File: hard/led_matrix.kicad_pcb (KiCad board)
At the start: 2 copper layers, 1 part

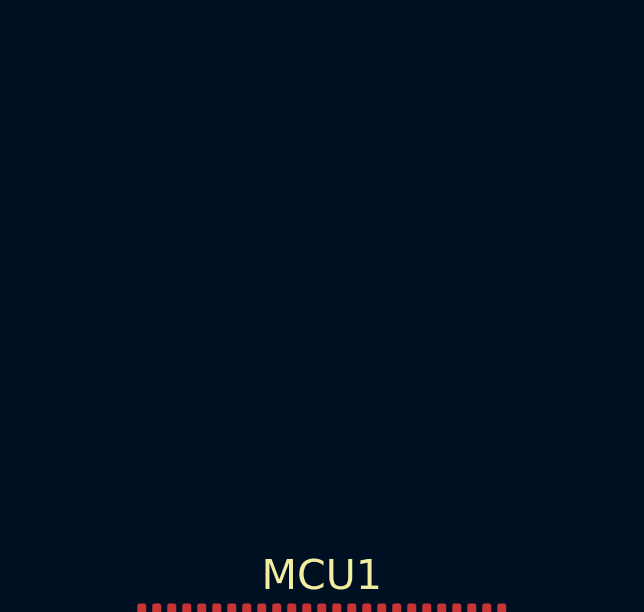
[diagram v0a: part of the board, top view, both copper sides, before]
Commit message: added 3d model for dc dc inductor
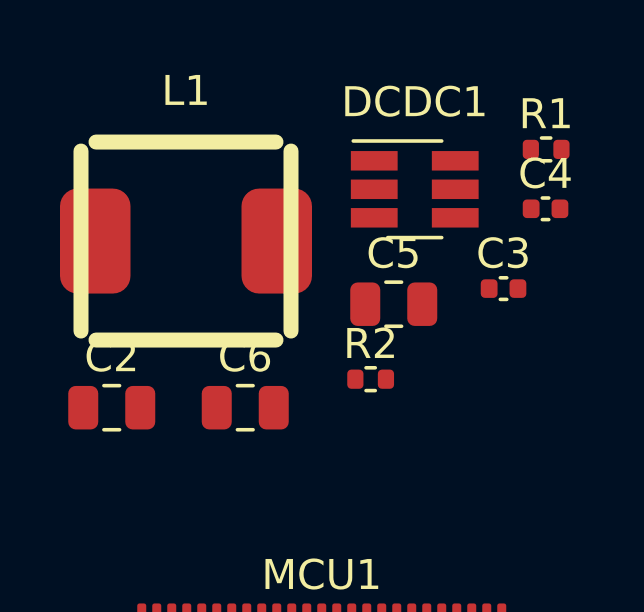
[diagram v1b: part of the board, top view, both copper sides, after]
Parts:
- added C2: 22u/16V, Capacitor_SMD:C_0805_2012Metric, F.Cu at (115.0, 70.0)
- added C3: 100n/16V, Capacitor_SMD:C_0402_1005Metric, F.Cu at (128.1, 66.0)
- added C4: 68p, Capacitor_SMD:C_0402_1005Metric, F.Cu at (129.5, 63.4)
- added C5: 22u/16V, Capacitor_SMD:C_0805_2012Metric, F.Cu at (124.4, 66.5)
- added C6: 22u/16V, Capacitor_SMD:C_0805_2012Metric, F.Cu at (119.5, 70.0)
- added DCDC1: TPS54302DDCR, Package_TO_SOT_SMD:SOT-23-6_Handsoldering, F.Cu at (125.1, 62.7)
- added L1: 8u2, led_matrix:L_Sunking_MWSA0603S, F.Cu at (117.5, 64.4)
- added R1: 100K/1%, Resistor_SMD:R_0402_1005Metric, F.Cu at (129.5, 61.4)
- added R2: 22K/1%, Resistor_SMD:R_0402_1005Metric, F.Cu at (123.6, 69.0)

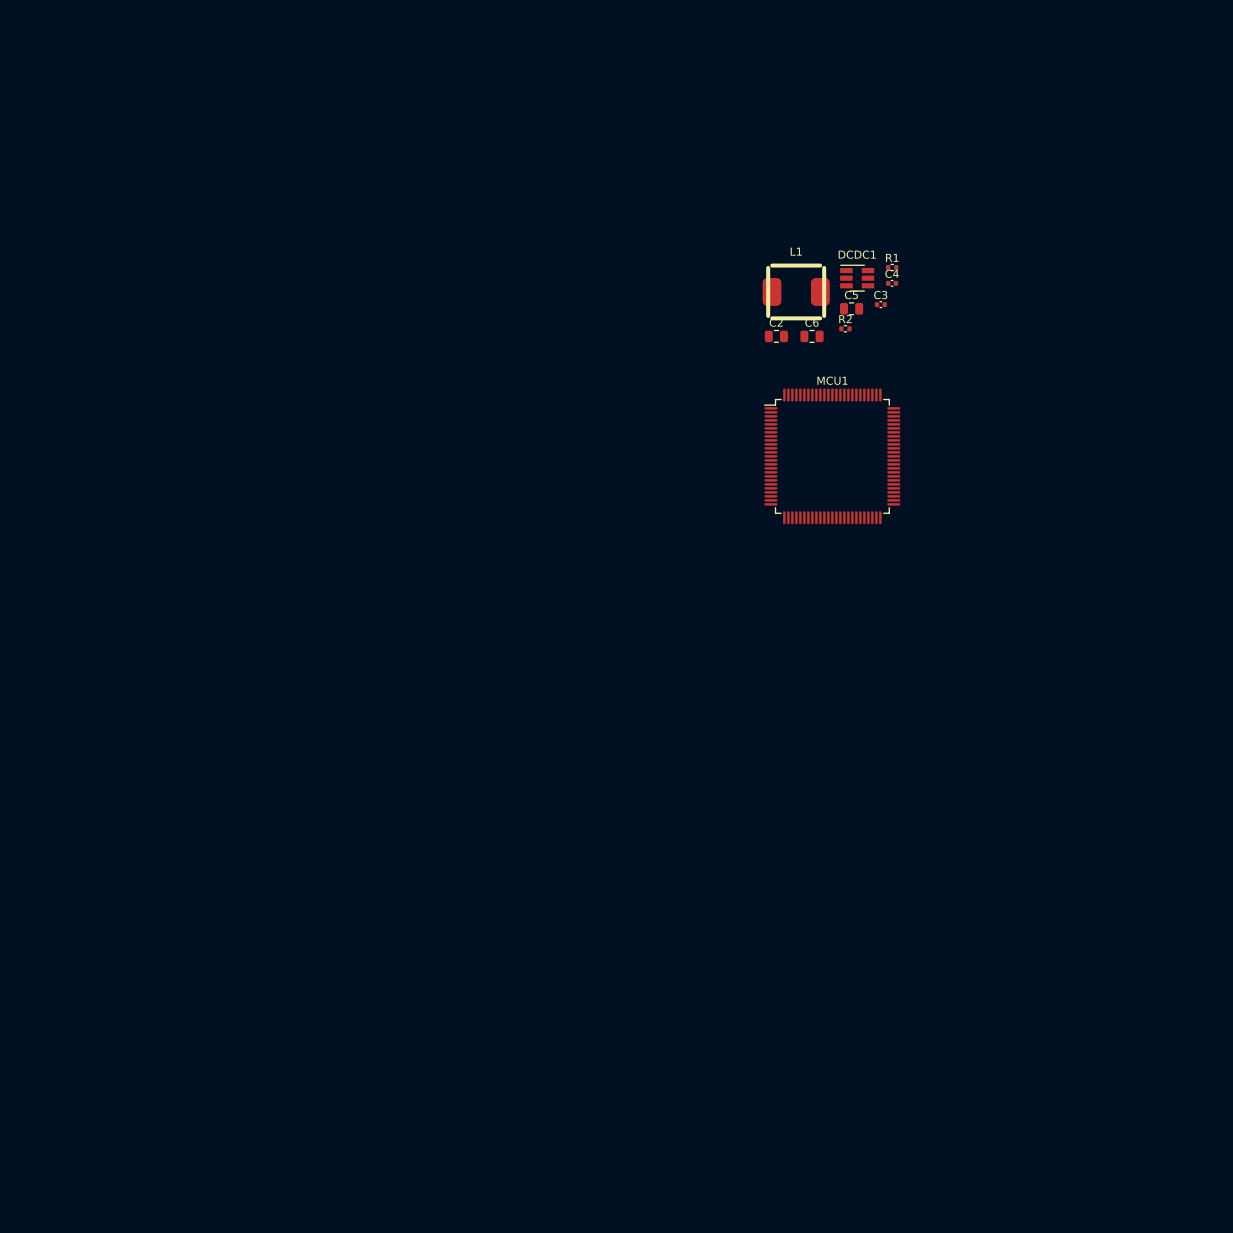
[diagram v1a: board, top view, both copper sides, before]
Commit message: signal nmos added
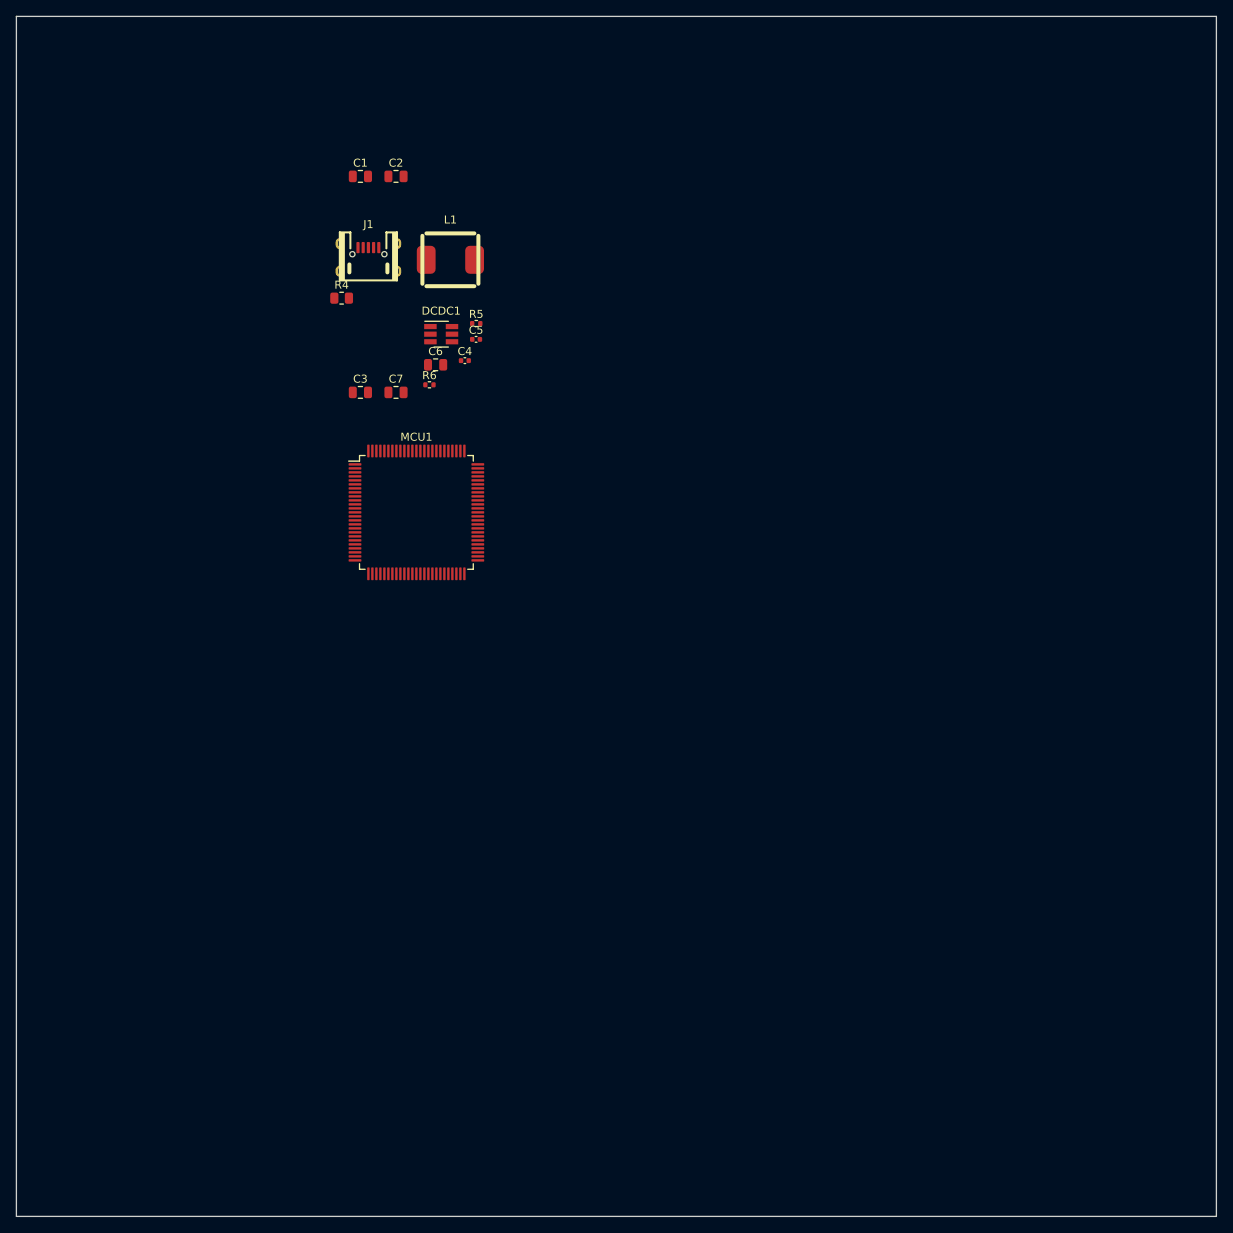
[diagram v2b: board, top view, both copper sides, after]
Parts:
- removed R1: 100K/1%, Resistor_SMD:R_0402_1005Metric
- removed R2: 22K/1%, Resistor_SMD:R_0402_1005Metric
- added C1: 22u/16V, Capacitor_SMD:C_0805_2012Metric, F.Cu at (63.0, 50.0)
- added C7: 22u/16V, Capacitor_SMD:C_0805_2012Metric, F.Cu at (67.5, 77.0)
- added J1: MicroXNJ, led_matrix:Connectors_SHOU HAN_MICRO 4P DIP, F.Cu at (64.0, 63.0)
- added R4: 0R1, Resistor_SMD:R_0805_2012Metric, F.Cu at (60.7, 65.2)
- added R5: 100K/1%, Resistor_SMD:R_0402_1005Metric, F.Cu at (77.5, 68.4)
- added R6: 22K/1%, Resistor_SMD:R_0402_1005Metric, F.Cu at (71.6, 76.0)
- C3: value 100n/16V -> 22u/16V; footprint Capacitor_SMD:C_0402_1005Metric -> Capacitor_SMD:C_0805_2012Metric
- C4: value 68p -> 100n/16V
- C5: value 22u/16V -> 68p; footprint Capacitor_SMD:C_0805_2012Metric -> Capacitor_SMD:C_0402_1005Metric
- moved C3 66.0 mm to (63.0, 77.0)
- moved C4 54.3 mm to (76.1, 73.0)
- moved DCDC1 52.5 mm to (73.1, 69.7)
- moved MCU1 52.5 mm to (70.0, 92.0)
- moved C2 51.6 mm to (67.5, 50.0)
- moved C6 47.2 mm to (72.4, 73.5)
- moved C5 47.1 mm to (77.5, 70.4)
- moved L1 43.4 mm to (74.2, 60.4)
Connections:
- C3 pad 1: Net-(C3-Pad1) -> GND
- C3 pad 2: Net-(C3-Pad2) -> +5V
- C4 pad 2: +3V3 -> Net-(C4-Pad2)
- C5 pad 1: GND -> Net-(C5-Pad1)
- DCDC1 pad 2: Net-(C3-Pad1) -> Net-(C4-Pad1)
- DCDC1 pad 4: Net-(C4-Pad1) -> Net-(C5-Pad1)
- DCDC1 pad 6: Net-(C3-Pad2) -> Net-(C4-Pad2)
- L1 pad 1: Net-(C3-Pad1) -> Net-(C4-Pad1)
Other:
- board outline added: 150 x 150 mm

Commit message: RIIIIIIIIIIIIIBSSSSSS!!!!
Rib break
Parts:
- added D1: LTST-S270TBKT, led_matrix:LED_LiteOn_LTST-S270TBKT, F.Cu at (74.3, 177.2)
- added D10: LTST-S270TBKT, led_matrix:LED_LiteOn_LTST-S270TBKT, F.Cu at (52.3, 137.3)
- added D100: LTST-S270TBKT, led_matrix:LED_LiteOn_LTST-S270TBKT, F.Cu at (78.7, 139.4)
- added D1000: LTST-S270TBKT, led_matrix:LED_LiteOn_LTST-S270TBKT, F.Cu at (179.9, 154.1)
- added D1001: LTST-S270TBKT, led_matrix:LED_LiteOn_LTST-S270TBKT, F.Cu at (175.5, 158.3)
- added D1002: LTST-S270TBKT, led_matrix:LED_LiteOn_LTST-S270TBKT, F.Cu at (171.1, 162.5)
- added D1003: LTST-S270TBKT, led_matrix:LED_LiteOn_LTST-S270TBKT, F.Cu at (166.7, 166.7)
- added D1004: LTST-S270TBKT, led_matrix:LED_LiteOn_LTST-S270TBKT, F.Cu at (162.3, 170.9)
- added D1005: LTST-S270TBKT, led_matrix:LED_LiteOn_LTST-S270TBKT, F.Cu at (157.9, 175.1)
- added D1006: LTST-S270TBKT, led_matrix:LED_LiteOn_LTST-S270TBKT, F.Cu at (153.5, 179.3)
- added D1007: LTST-S270TBKT, led_matrix:LED_LiteOn_LTST-S270TBKT, F.Cu at (122.7, 210.8)
- added D1008: LTST-S270TBKT, led_matrix:LED_LiteOn_LTST-S270TBKT, F.Cu at (127.1, 206.6)
- added D1009: LTST-S270TBKT, led_matrix:LED_LiteOn_LTST-S270TBKT, F.Cu at (113.9, 210.8)
- added D101: LTST-S270TBKT, led_matrix:LED_LiteOn_LTST-S270TBKT, F.Cu at (83.1, 137.3)
- added D1010: LTST-S270TBKT, led_matrix:LED_LiteOn_LTST-S270TBKT, F.Cu at (135.9, 198.2)
- added D1011: LTST-S270TBKT, led_matrix:LED_LiteOn_LTST-S270TBKT, F.Cu at (140.3, 194.0)
- added D1012: LTST-S270TBKT, led_matrix:LED_LiteOn_LTST-S270TBKT, F.Cu at (144.7, 189.8)
- added D1013: LTST-S270TBKT, led_matrix:LED_LiteOn_LTST-S270TBKT, F.Cu at (149.1, 185.6)
- added D1014: LTST-S270TBKT, led_matrix:LED_LiteOn_LTST-S270TBKT, F.Cu at (149.1, 187.7)
- added D1015: LTST-S270TBKT, led_matrix:LED_LiteOn_LTST-S270TBKT, F.Cu at (144.7, 191.9)
- added D1016: LTST-S270TBKT, led_matrix:LED_LiteOn_LTST-S270TBKT, F.Cu at (140.3, 196.1)
- added D1017: LTST-S270TBKT, led_matrix:LED_LiteOn_LTST-S270TBKT, F.Cu at (135.9, 200.3)
- added D1018: LTST-S270TBKT, led_matrix:LED_LiteOn_LTST-S270TBKT, F.Cu at (131.5, 204.5)
- added D1019: LTST-S270TBKT, led_matrix:LED_LiteOn_LTST-S270TBKT, F.Cu at (127.1, 208.7)
- added D102: LTST-S270TBKT, led_matrix:LED_LiteOn_LTST-S270TBKT, F.Cu at (78.7, 141.5)
- added D1020: LTST-S270TBKT, led_matrix:LED_LiteOn_LTST-S270TBKT, F.Cu at (122.7, 212.9)
- added D1021: LTST-S270TBKT, led_matrix:LED_LiteOn_LTST-S270TBKT, F.Cu at (153.5, 181.4)
- added D1022: LTST-S270TBKT, led_matrix:LED_LiteOn_LTST-S270TBKT, F.Cu at (157.9, 177.2)
- added D1023: LTST-S270TBKT, led_matrix:LED_LiteOn_LTST-S270TBKT, F.Cu at (162.3, 173.0)
- added D1024: LTST-S270TBKT, led_matrix:LED_LiteOn_LTST-S270TBKT, F.Cu at (166.7, 168.8)
- added D103: LTST-S270TBKT, led_matrix:LED_LiteOn_LTST-S270TBKT, F.Cu at (74.3, 145.7)
- added D104: LTST-S270TBKT, led_matrix:LED_LiteOn_LTST-S270TBKT, F.Cu at (69.9, 149.9)
- added D105: LTST-S270TBKT, led_matrix:LED_LiteOn_LTST-S270TBKT, F.Cu at (65.5, 154.1)
- added D106: LTST-S270TBKT, led_matrix:LED_LiteOn_LTST-S270TBKT, F.Cu at (61.1, 158.3)
- added D107: LTST-S270TBKT, led_matrix:LED_LiteOn_LTST-S270TBKT, F.Cu at (56.7, 162.5)
- added D108: LTST-S270TBKT, led_matrix:LED_LiteOn_LTST-S270TBKT, F.Cu at (52.3, 166.7)
- added D109: LTST-S270TBKT, led_matrix:LED_LiteOn_LTST-S270TBKT, F.Cu at (47.9, 170.9)
- added D11: LTST-S270TBKT, led_matrix:LED_LiteOn_LTST-S270TBKT, F.Cu at (47.9, 141.5)
- added D110: LTST-S270TBKT, led_matrix:LED_LiteOn_LTST-S270TBKT, F.Cu at (25.7, 120.5)
- added D111: LTST-S270TBKT, led_matrix:LED_LiteOn_LTST-S270TBKT, F.Cu at (87.5, 135.2)
- added D112: LTST-S270TBKT, led_matrix:LED_LiteOn_LTST-S270TBKT, F.Cu at (25.7, 125.0)
- added D113: LTST-S270TBKT, led_matrix:LED_LiteOn_LTST-S270TBKT, F.Cu at (65.5, 139.4)
- added D114: LTST-S270TBKT, led_matrix:LED_LiteOn_LTST-S270TBKT, F.Cu at (52.3, 168.8)
- added D115: LTST-S270TBKT, led_matrix:LED_LiteOn_LTST-S270TBKT, F.Cu at (56.7, 164.6)
- added D116: LTST-S270TBKT, led_matrix:LED_LiteOn_LTST-S270TBKT, F.Cu at (61.1, 160.4)
- added D117: LTST-S270TBKT, led_matrix:LED_LiteOn_LTST-S270TBKT, F.Cu at (65.5, 156.2)
- added D118: LTST-S270TBKT, led_matrix:LED_LiteOn_LTST-S270TBKT, F.Cu at (69.9, 152.0)
- added D119: LTST-S270TBKT, led_matrix:LED_LiteOn_LTST-S270TBKT, F.Cu at (74.3, 147.8)
- added D12: LTST-S270TBKT, led_matrix:LED_LiteOn_LTST-S270TBKT, F.Cu at (25.7, 57.0)
- added D120: LTST-S270TBKT, led_matrix:LED_LiteOn_LTST-S270TBKT, F.Cu at (78.7, 143.6)
- added D121: LTST-S270TBKT, led_matrix:LED_LiteOn_LTST-S270TBKT, F.Cu at (83.1, 139.4)
- added D122: LTST-S270TBKT, led_matrix:LED_LiteOn_LTST-S270TBKT, F.Cu at (87.5, 137.3)
- added D123: LTST-S270TBKT, led_matrix:LED_LiteOn_LTST-S270TBKT, F.Cu at (83.1, 141.5)
- added D124: LTST-S270TBKT, led_matrix:LED_LiteOn_LTST-S270TBKT, F.Cu at (78.7, 145.7)
- added D125: LTST-S270TBKT, led_matrix:LED_LiteOn_LTST-S270TBKT, F.Cu at (74.3, 149.9)
- added D126: LTST-S270TBKT, led_matrix:LED_LiteOn_LTST-S270TBKT, F.Cu at (69.9, 154.1)
- added D127: LTST-S270TBKT, led_matrix:LED_LiteOn_LTST-S270TBKT, F.Cu at (65.5, 158.3)
- added D128: LTST-S270TBKT, led_matrix:LED_LiteOn_LTST-S270TBKT, F.Cu at (61.1, 162.5)
- added D129: LTST-S270TBKT, led_matrix:LED_LiteOn_LTST-S270TBKT, F.Cu at (74.3, 160.4)
- added D13: LTST-S270TBKT, led_matrix:LED_LiteOn_LTST-S270TBKT, F.Cu at (56.7, 135.2)
- added D130: LTST-S270TBKT, led_matrix:LED_LiteOn_LTST-S270TBKT, F.Cu at (52.3, 170.9)
- added D131: LTST-S270TBKT, led_matrix:LED_LiteOn_LTST-S270TBKT, F.Cu at (47.9, 175.1)
- added D132: LTST-S270TBKT, led_matrix:LED_LiteOn_LTST-S270TBKT, F.Cu at (25.7, 129.5)
- added D133: LTST-S270TBKT, led_matrix:LED_LiteOn_LTST-S270TBKT, F.Cu at (91.9, 135.2)
- added D134: LTST-S270TBKT, led_matrix:LED_LiteOn_LTST-S270TBKT, F.Cu at (25.7, 134.1)
- added D135: LTST-S270TBKT, led_matrix:LED_LiteOn_LTST-S270TBKT, F.Cu at (47.9, 177.2)
- added D136: LTST-S270TBKT, led_matrix:LED_LiteOn_LTST-S270TBKT, F.Cu at (52.3, 173.0)
- added D137: LTST-S270TBKT, led_matrix:LED_LiteOn_LTST-S270TBKT, F.Cu at (56.7, 168.8)
- added D138: LTST-S270TBKT, led_matrix:LED_LiteOn_LTST-S270TBKT, F.Cu at (61.1, 164.6)
- added D139: LTST-S270TBKT, led_matrix:LED_LiteOn_LTST-S270TBKT, F.Cu at (65.5, 160.4)
- added D14: LTST-S270TBKT, led_matrix:LED_LiteOn_LTST-S270TBKT, F.Cu at (25.7, 61.5)
- added D140: LTST-S270TBKT, led_matrix:LED_LiteOn_LTST-S270TBKT, F.Cu at (69.9, 156.2)
- added D141: LTST-S270TBKT, led_matrix:LED_LiteOn_LTST-S270TBKT, F.Cu at (74.3, 152.0)
- added D142: LTST-S270TBKT, led_matrix:LED_LiteOn_LTST-S270TBKT, F.Cu at (78.7, 147.8)
- added D143: LTST-S270TBKT, led_matrix:LED_LiteOn_LTST-S270TBKT, F.Cu at (83.1, 143.6)
- added D144: LTST-S270TBKT, led_matrix:LED_LiteOn_LTST-S270TBKT, F.Cu at (87.5, 139.4)
- added D145: LTST-S270TBKT, led_matrix:LED_LiteOn_LTST-S270TBKT, F.Cu at (91.9, 137.3)
- added D146: LTST-S270TBKT, led_matrix:LED_LiteOn_LTST-S270TBKT, F.Cu at (87.5, 141.5)
- added D147: LTST-S270TBKT, led_matrix:LED_LiteOn_LTST-S270TBKT, F.Cu at (83.1, 145.7)
- added D148: LTST-S270TBKT, led_matrix:LED_LiteOn_LTST-S270TBKT, F.Cu at (78.7, 149.9)
- added D149: LTST-S270TBKT, led_matrix:LED_LiteOn_LTST-S270TBKT, F.Cu at (74.3, 154.1)
- added D15: LTST-S270TBKT, led_matrix:LED_LiteOn_LTST-S270TBKT, F.Cu at (47.9, 143.6)
- added D150: LTST-S270TBKT, led_matrix:LED_LiteOn_LTST-S270TBKT, F.Cu at (69.9, 158.3)
- added D151: LTST-S270TBKT, led_matrix:LED_LiteOn_LTST-S270TBKT, F.Cu at (65.5, 162.5)
- added D152: LTST-S270TBKT, led_matrix:LED_LiteOn_LTST-S270TBKT, F.Cu at (61.1, 166.7)
- added D153: LTST-S270TBKT, led_matrix:LED_LiteOn_LTST-S270TBKT, F.Cu at (56.7, 170.9)
- added D154: LTST-S270TBKT, led_matrix:LED_LiteOn_LTST-S270TBKT, F.Cu at (52.3, 175.1)
- added D155: LTST-S270TBKT, led_matrix:LED_LiteOn_LTST-S270TBKT, F.Cu at (47.9, 179.3)
- added D156: LTST-S270TBKT, led_matrix:LED_LiteOn_LTST-S270TBKT, F.Cu at (25.7, 138.6)
- added D157: LTST-S270TBKT, led_matrix:LED_LiteOn_LTST-S270TBKT, F.Cu at (25.7, 143.1)
- added D158: LTST-S270TBKT, led_matrix:LED_LiteOn_LTST-S270TBKT, F.Cu at (96.3, 135.2)
- added D159: LTST-S270TBKT, led_matrix:LED_LiteOn_LTST-S270TBKT, F.Cu at (25.7, 147.7)
- added D16: LTST-S270TBKT, led_matrix:LED_LiteOn_LTST-S270TBKT, F.Cu at (52.3, 139.4)
- added D160: LTST-S270TBKT, led_matrix:LED_LiteOn_LTST-S270TBKT, F.Cu at (47.9, 181.4)
- added D161: LTST-S270TBKT, led_matrix:LED_LiteOn_LTST-S270TBKT, F.Cu at (52.3, 177.2)
- added D162: LTST-S270TBKT, led_matrix:LED_LiteOn_LTST-S270TBKT, F.Cu at (56.7, 173.0)
- added D163: LTST-S270TBKT, led_matrix:LED_LiteOn_LTST-S270TBKT, F.Cu at (61.1, 168.8)
- added D164: LTST-S270TBKT, led_matrix:LED_LiteOn_LTST-S270TBKT, F.Cu at (65.5, 164.6)
- added D165: LTST-S270TBKT, led_matrix:LED_LiteOn_LTST-S270TBKT, F.Cu at (69.9, 160.4)
- added D166: LTST-S270TBKT, led_matrix:LED_LiteOn_LTST-S270TBKT, F.Cu at (74.3, 156.2)
- added D167: LTST-S270TBKT, led_matrix:LED_LiteOn_LTST-S270TBKT, F.Cu at (78.7, 152.0)
- added D168: LTST-S270TBKT, led_matrix:LED_LiteOn_LTST-S270TBKT, F.Cu at (83.1, 147.8)
- added D169: LTST-S270TBKT, led_matrix:LED_LiteOn_LTST-S270TBKT, F.Cu at (87.5, 143.6)
- added D17: LTST-S270TBKT, led_matrix:LED_LiteOn_LTST-S270TBKT, F.Cu at (56.7, 137.3)
- added D170: LTST-S270TBKT, led_matrix:LED_LiteOn_LTST-S270TBKT, F.Cu at (91.9, 139.4)
- added D171: LTST-S270TBKT, led_matrix:LED_LiteOn_LTST-S270TBKT, F.Cu at (96.3, 137.3)
- added D172: LTST-S270TBKT, led_matrix:LED_LiteOn_LTST-S270TBKT, F.Cu at (91.9, 141.5)
- added D173: LTST-S270TBKT, led_matrix:LED_LiteOn_LTST-S270TBKT, F.Cu at (87.5, 145.7)
- added D174: LTST-S270TBKT, led_matrix:LED_LiteOn_LTST-S270TBKT, F.Cu at (83.1, 149.9)
- added D175: LTST-S270TBKT, led_matrix:LED_LiteOn_LTST-S270TBKT, F.Cu at (78.7, 154.1)
- added D176: LTST-S270TBKT, led_matrix:LED_LiteOn_LTST-S270TBKT, F.Cu at (74.3, 158.3)
- added D177: LTST-S270TBKT, led_matrix:LED_LiteOn_LTST-S270TBKT, F.Cu at (69.9, 202.4)
- added D178: LTST-S270TBKT, led_matrix:LED_LiteOn_LTST-S270TBKT, F.Cu at (65.5, 166.7)
- added D179: LTST-S270TBKT, led_matrix:LED_LiteOn_LTST-S270TBKT, F.Cu at (61.1, 170.9)
- added D18: LTST-S270TBKT, led_matrix:LED_LiteOn_LTST-S270TBKT, F.Cu at (52.3, 141.5)
- added D180: LTST-S270TBKT, led_matrix:LED_LiteOn_LTST-S270TBKT, F.Cu at (56.7, 175.1)
- added D181: LTST-S270TBKT, led_matrix:LED_LiteOn_LTST-S270TBKT, F.Cu at (52.3, 179.3)
- added D182: LTST-S270TBKT, led_matrix:LED_LiteOn_LTST-S270TBKT, F.Cu at (47.9, 183.5)
- added D183: LTST-S270TBKT, led_matrix:LED_LiteOn_LTST-S270TBKT, F.Cu at (25.7, 152.2)
- added D184: LTST-S270TBKT, led_matrix:LED_LiteOn_LTST-S270TBKT, F.Cu at (47.9, 185.6)
- added D185: LTST-S270TBKT, led_matrix:LED_LiteOn_LTST-S270TBKT, F.Cu at (100.7, 135.2)
- added D186: LTST-S270TBKT, led_matrix:LED_LiteOn_LTST-S270TBKT, F.Cu at (47.9, 187.7)
- added D187: LTST-S270TBKT, led_matrix:LED_LiteOn_LTST-S270TBKT, F.Cu at (25.7, 156.7)
- added D188: LTST-S270TBKT, led_matrix:LED_LiteOn_LTST-S270TBKT, F.Cu at (52.3, 181.4)
- added D189: LTST-S270TBKT, led_matrix:LED_LiteOn_LTST-S270TBKT, F.Cu at (56.7, 177.2)
- added D19: LTST-S270TBKT, led_matrix:LED_LiteOn_LTST-S270TBKT, F.Cu at (47.9, 145.7)
- added D190: LTST-S270TBKT, led_matrix:LED_LiteOn_LTST-S270TBKT, F.Cu at (61.1, 173.0)
- added D191: LTST-S270TBKT, led_matrix:LED_LiteOn_LTST-S270TBKT, F.Cu at (65.5, 168.8)
- added D192: LTST-S270TBKT, led_matrix:LED_LiteOn_LTST-S270TBKT, F.Cu at (69.9, 164.6)
- added D193: LTST-S270TBKT, led_matrix:LED_LiteOn_LTST-S270TBKT, F.Cu at (56.7, 166.7)
- added D194: LTST-S270TBKT, led_matrix:LED_LiteOn_LTST-S270TBKT, F.Cu at (78.7, 156.2)
- added D195: LTST-S270TBKT, led_matrix:LED_LiteOn_LTST-S270TBKT, F.Cu at (83.1, 152.0)
- added D196: LTST-S270TBKT, led_matrix:LED_LiteOn_LTST-S270TBKT, F.Cu at (87.5, 147.8)
- added D197: LTST-S270TBKT, led_matrix:LED_LiteOn_LTST-S270TBKT, F.Cu at (91.9, 143.6)
- added D198: LTST-S270TBKT, led_matrix:LED_LiteOn_LTST-S270TBKT, F.Cu at (96.3, 139.4)
- added D199: LTST-S270TBKT, led_matrix:LED_LiteOn_LTST-S270TBKT, F.Cu at (100.7, 137.3)
- added D2: LTST-S270TBKT, led_matrix:LED_LiteOn_LTST-S270TBKT, F.Cu at (25.7, 38.8)
- added D20: LTST-S270TBKT, led_matrix:LED_LiteOn_LTST-S270TBKT, F.Cu at (25.7, 66.0)
- added D200: LTST-S270TBKT, led_matrix:LED_LiteOn_LTST-S270TBKT, F.Cu at (96.3, 141.5)
- added D201: LTST-S270TBKT, led_matrix:LED_LiteOn_LTST-S270TBKT, F.Cu at (91.9, 145.7)
- added D202: LTST-S270TBKT, led_matrix:LED_LiteOn_LTST-S270TBKT, F.Cu at (87.5, 149.9)
- added D203: LTST-S270TBKT, led_matrix:LED_LiteOn_LTST-S270TBKT, F.Cu at (83.1, 154.1)
- added D204: LTST-S270TBKT, led_matrix:LED_LiteOn_LTST-S270TBKT, F.Cu at (78.7, 158.3)
- added D205: LTST-S270TBKT, led_matrix:LED_LiteOn_LTST-S270TBKT, F.Cu at (74.3, 162.5)
- added D206: LTST-S270TBKT, led_matrix:LED_LiteOn_LTST-S270TBKT, F.Cu at (69.9, 166.7)
- added D207: LTST-S270TBKT, led_matrix:LED_LiteOn_LTST-S270TBKT, F.Cu at (65.5, 170.9)
- added D208: LTST-S270TBKT, led_matrix:LED_LiteOn_LTST-S270TBKT, F.Cu at (61.1, 175.1)
- added D209: LTST-S270TBKT, led_matrix:LED_LiteOn_LTST-S270TBKT, F.Cu at (56.7, 179.3)
- added D21: LTST-S270TBKT, led_matrix:LED_LiteOn_LTST-S270TBKT, F.Cu at (61.1, 135.2)
- added D210: LTST-S270TBKT, led_matrix:LED_LiteOn_LTST-S270TBKT, F.Cu at (52.3, 183.5)
- added D211: LTST-S270TBKT, led_matrix:LED_LiteOn_LTST-S270TBKT, F.Cu at (25.7, 161.3)
- added D212: LTST-S270TBKT, led_matrix:LED_LiteOn_LTST-S270TBKT, F.Cu at (47.9, 189.8)
- added D213: LTST-S270TBKT, led_matrix:LED_LiteOn_LTST-S270TBKT, F.Cu at (52.3, 185.6)
- added D214: LTST-S270TBKT, led_matrix:LED_LiteOn_LTST-S270TBKT, F.Cu at (105.1, 135.2)
- added D215: LTST-S270TBKT, led_matrix:LED_LiteOn_LTST-S270TBKT, F.Cu at (52.3, 187.7)
- added D216: LTST-S270TBKT, led_matrix:LED_LiteOn_LTST-S270TBKT, F.Cu at (47.9, 191.9)
- added D217: LTST-S270TBKT, led_matrix:LED_LiteOn_LTST-S270TBKT, F.Cu at (25.7, 165.8)
- added D218: LTST-S270TBKT, led_matrix:LED_LiteOn_LTST-S270TBKT, F.Cu at (56.7, 181.4)
- added D219: LTST-S270TBKT, led_matrix:LED_LiteOn_LTST-S270TBKT, F.Cu at (61.1, 177.2)
- added D22: LTST-S270TBKT, led_matrix:LED_LiteOn_LTST-S270TBKT, F.Cu at (25.7, 70.6)
- added D220: LTST-S270TBKT, led_matrix:LED_LiteOn_LTST-S270TBKT, F.Cu at (65.5, 173.0)
- added D221: LTST-S270TBKT, led_matrix:LED_LiteOn_LTST-S270TBKT, F.Cu at (69.9, 168.8)
- added D222: LTST-S270TBKT, led_matrix:LED_LiteOn_LTST-S270TBKT, F.Cu at (74.3, 164.6)
- added D223: LTST-S270TBKT, led_matrix:LED_LiteOn_LTST-S270TBKT, F.Cu at (78.7, 160.4)
- added D224: LTST-S270TBKT, led_matrix:LED_LiteOn_LTST-S270TBKT, F.Cu at (83.1, 156.2)
- added D225: LTST-S270TBKT, led_matrix:LED_LiteOn_LTST-S270TBKT, F.Cu at (87.5, 152.0)
- added D226: LTST-S270TBKT, led_matrix:LED_LiteOn_LTST-S270TBKT, F.Cu at (91.9, 147.8)
- added D227: LTST-S270TBKT, led_matrix:LED_LiteOn_LTST-S270TBKT, F.Cu at (96.3, 143.6)
- added D228: LTST-S270TBKT, led_matrix:LED_LiteOn_LTST-S270TBKT, F.Cu at (100.7, 139.4)
- added D229: LTST-S270TBKT, led_matrix:LED_LiteOn_LTST-S270TBKT, F.Cu at (105.1, 137.3)
- added D23: LTST-S270TBKT, led_matrix:LED_LiteOn_LTST-S270TBKT, F.Cu at (47.9, 147.8)
- added D230: LTST-S270TBKT, led_matrix:LED_LiteOn_LTST-S270TBKT, F.Cu at (100.7, 141.5)
- added D231: LTST-S270TBKT, led_matrix:LED_LiteOn_LTST-S270TBKT, F.Cu at (96.3, 145.7)
- added D232: LTST-S270TBKT, led_matrix:LED_LiteOn_LTST-S270TBKT, F.Cu at (91.9, 149.9)
- added D233: LTST-S270TBKT, led_matrix:LED_LiteOn_LTST-S270TBKT, F.Cu at (87.5, 154.1)
- added D234: LTST-S270TBKT, led_matrix:LED_LiteOn_LTST-S270TBKT, F.Cu at (83.1, 158.3)
- added D235: LTST-S270TBKT, led_matrix:LED_LiteOn_LTST-S270TBKT, F.Cu at (78.7, 162.5)
- added D236: LTST-S270TBKT, led_matrix:LED_LiteOn_LTST-S270TBKT, F.Cu at (74.3, 166.7)
- added D237: LTST-S270TBKT, led_matrix:LED_LiteOn_LTST-S270TBKT, F.Cu at (69.9, 170.9)
- added D238: LTST-S270TBKT, led_matrix:LED_LiteOn_LTST-S270TBKT, F.Cu at (65.5, 175.1)
- added D239: LTST-S270TBKT, led_matrix:LED_LiteOn_LTST-S270TBKT, F.Cu at (61.1, 179.3)
- added D24: LTST-S270TBKT, led_matrix:LED_LiteOn_LTST-S270TBKT, F.Cu at (52.3, 143.6)
- added D240: LTST-S270TBKT, led_matrix:LED_LiteOn_LTST-S270TBKT, F.Cu at (56.7, 183.5)
- added D241: LTST-S270TBKT, led_matrix:LED_LiteOn_LTST-S270TBKT, F.Cu at (69.9, 162.5)
- added D242: LTST-S270TBKT, led_matrix:LED_LiteOn_LTST-S270TBKT, F.Cu at (47.9, 194.0)
- added D243: LTST-S270TBKT, led_matrix:LED_LiteOn_LTST-S270TBKT, F.Cu at (52.3, 189.8)
- added D244: LTST-S270TBKT, led_matrix:LED_LiteOn_LTST-S270TBKT, F.Cu at (56.7, 185.6)
- added D245: LTST-S270TBKT, led_matrix:LED_LiteOn_LTST-S270TBKT, F.Cu at (109.5, 135.2)
- added D246: LTST-S270TBKT, led_matrix:LED_LiteOn_LTST-S270TBKT, F.Cu at (56.7, 187.7)
- added D247: LTST-S270TBKT, led_matrix:LED_LiteOn_LTST-S270TBKT, F.Cu at (52.3, 191.9)
- added D248: LTST-S270TBKT, led_matrix:LED_LiteOn_LTST-S270TBKT, F.Cu at (47.9, 196.1)
- added D249: LTST-S270TBKT, led_matrix:LED_LiteOn_LTST-S270TBKT, F.Cu at (25.7, 174.9)
- added D25: LTST-S270TBKT, led_matrix:LED_LiteOn_LTST-S270TBKT, F.Cu at (56.7, 139.4)
- added D250: LTST-S270TBKT, led_matrix:LED_LiteOn_LTST-S270TBKT, F.Cu at (61.1, 181.4)
- added D251: LTST-S270TBKT, led_matrix:LED_LiteOn_LTST-S270TBKT, F.Cu at (65.5, 177.2)
- added D252: LTST-S270TBKT, led_matrix:LED_LiteOn_LTST-S270TBKT, F.Cu at (69.9, 173.0)
- added D253: LTST-S270TBKT, led_matrix:LED_LiteOn_LTST-S270TBKT, F.Cu at (74.3, 168.8)
- added D254: LTST-S270TBKT, led_matrix:LED_LiteOn_LTST-S270TBKT, F.Cu at (78.7, 164.6)
- added D255: LTST-S270TBKT, led_matrix:LED_LiteOn_LTST-S270TBKT, F.Cu at (83.1, 160.4)
- added D256: LTST-S270TBKT, led_matrix:LED_LiteOn_LTST-S270TBKT, F.Cu at (87.5, 156.2)
- added D257: LTST-S270TBKT, led_matrix:LED_LiteOn_LTST-S270TBKT, F.Cu at (74.3, 137.3)
- added D258: LTST-S270TBKT, led_matrix:LED_LiteOn_LTST-S270TBKT, F.Cu at (96.3, 147.8)
- added D259: LTST-S270TBKT, led_matrix:LED_LiteOn_LTST-S270TBKT, F.Cu at (100.7, 143.6)
- added D26: LTST-S270TBKT, led_matrix:LED_LiteOn_LTST-S270TBKT, F.Cu at (61.1, 137.3)
- added D260: LTST-S270TBKT, led_matrix:LED_LiteOn_LTST-S270TBKT, F.Cu at (105.1, 139.4)
- added D261: LTST-S270TBKT, led_matrix:LED_LiteOn_LTST-S270TBKT, F.Cu at (109.5, 137.3)
- added D262: LTST-S270TBKT, led_matrix:LED_LiteOn_LTST-S270TBKT, F.Cu at (105.1, 141.5)
- added D263: LTST-S270TBKT, led_matrix:LED_LiteOn_LTST-S270TBKT, F.Cu at (100.7, 145.7)
- added D264: LTST-S270TBKT, led_matrix:LED_LiteOn_LTST-S270TBKT, F.Cu at (96.3, 149.9)
- added D265: LTST-S270TBKT, led_matrix:LED_LiteOn_LTST-S270TBKT, F.Cu at (91.9, 154.1)
- added D266: LTST-S270TBKT, led_matrix:LED_LiteOn_LTST-S270TBKT, F.Cu at (87.5, 158.3)
- added D267: LTST-S270TBKT, led_matrix:LED_LiteOn_LTST-S270TBKT, F.Cu at (83.1, 162.5)
- added D268: LTST-S270TBKT, led_matrix:LED_LiteOn_LTST-S270TBKT, F.Cu at (78.7, 166.7)
- added D269: LTST-S270TBKT, led_matrix:LED_LiteOn_LTST-S270TBKT, F.Cu at (74.3, 170.9)
- added D27: LTST-S270TBKT, led_matrix:LED_LiteOn_LTST-S270TBKT, F.Cu at (56.7, 141.5)
- added D270: LTST-S270TBKT, led_matrix:LED_LiteOn_LTST-S270TBKT, F.Cu at (69.9, 175.1)
- added D271: LTST-S270TBKT, led_matrix:LED_LiteOn_LTST-S270TBKT, F.Cu at (65.5, 179.3)
- added D272: LTST-S270TBKT, led_matrix:LED_LiteOn_LTST-S270TBKT, F.Cu at (61.1, 183.5)
- added D273: LTST-S270TBKT, led_matrix:LED_LiteOn_LTST-S270TBKT, F.Cu at (43.5, 202.4)
- added D274: LTST-S270TBKT, led_matrix:LED_LiteOn_LTST-S270TBKT, F.Cu at (47.9, 198.2)
- added D275: LTST-S270TBKT, led_matrix:LED_LiteOn_LTST-S270TBKT, F.Cu at (52.3, 194.0)
- added D276: LTST-S270TBKT, led_matrix:LED_LiteOn_LTST-S270TBKT, F.Cu at (56.7, 189.8)
- added D277: LTST-S270TBKT, led_matrix:LED_LiteOn_LTST-S270TBKT, F.Cu at (61.1, 185.6)
- added D278: LTST-S270TBKT, led_matrix:LED_LiteOn_LTST-S270TBKT, F.Cu at (113.9, 135.2)
- added D279: LTST-S270TBKT, led_matrix:LED_LiteOn_LTST-S270TBKT, F.Cu at (61.1, 187.7)
- added D28: LTST-S270TBKT, led_matrix:LED_LiteOn_LTST-S270TBKT, F.Cu at (52.3, 145.7)
- added D280: LTST-S270TBKT, led_matrix:LED_LiteOn_LTST-S270TBKT, F.Cu at (56.7, 191.9)
- added D281: LTST-S270TBKT, led_matrix:LED_LiteOn_LTST-S270TBKT, F.Cu at (52.3, 196.1)
- added D282: LTST-S270TBKT, led_matrix:LED_LiteOn_LTST-S270TBKT, F.Cu at (47.9, 200.3)
- added D283: LTST-S270TBKT, led_matrix:LED_LiteOn_LTST-S270TBKT, F.Cu at (43.5, 204.5)
- added D284: LTST-S270TBKT, led_matrix:LED_LiteOn_LTST-S270TBKT, F.Cu at (65.5, 181.4)
- added D285: LTST-S270TBKT, led_matrix:LED_LiteOn_LTST-S270TBKT, F.Cu at (69.9, 177.2)
- added D286: LTST-S270TBKT, led_matrix:LED_LiteOn_LTST-S270TBKT, F.Cu at (74.3, 173.0)
- added D287: LTST-S270TBKT, led_matrix:LED_LiteOn_LTST-S270TBKT, F.Cu at (78.7, 168.8)
- added D288: LTST-S270TBKT, led_matrix:LED_LiteOn_LTST-S270TBKT, F.Cu at (83.1, 164.6)
- added D289: LTST-S270TBKT, led_matrix:LED_LiteOn_LTST-S270TBKT, F.Cu at (87.5, 160.4)
- added D29: LTST-S270TBKT, led_matrix:LED_LiteOn_LTST-S270TBKT, F.Cu at (47.9, 149.9)
- added D290: LTST-S270TBKT, led_matrix:LED_LiteOn_LTST-S270TBKT, F.Cu at (91.9, 156.2)
- added D291: LTST-S270TBKT, led_matrix:LED_LiteOn_LTST-S270TBKT, F.Cu at (96.3, 152.0)
- added D292: LTST-S270TBKT, led_matrix:LED_LiteOn_LTST-S270TBKT, F.Cu at (100.7, 147.8)
- added D293: LTST-S270TBKT, led_matrix:LED_LiteOn_LTST-S270TBKT, F.Cu at (105.1, 143.6)
- added D294: LTST-S270TBKT, led_matrix:LED_LiteOn_LTST-S270TBKT, F.Cu at (109.5, 139.4)
- added D295: LTST-S270TBKT, led_matrix:LED_LiteOn_LTST-S270TBKT, F.Cu at (113.9, 137.3)
- added D296: LTST-S270TBKT, led_matrix:LED_LiteOn_LTST-S270TBKT, F.Cu at (109.5, 141.5)
- added D297: LTST-S270TBKT, led_matrix:LED_LiteOn_LTST-S270TBKT, F.Cu at (105.1, 145.7)
- added D298: LTST-S270TBKT, led_matrix:LED_LiteOn_LTST-S270TBKT, F.Cu at (100.7, 149.9)
- added D299: LTST-S270TBKT, led_matrix:LED_LiteOn_LTST-S270TBKT, F.Cu at (96.3, 154.1)
- added D3: LTST-S270TBKT, led_matrix:LED_LiteOn_LTST-S270TBKT, F.Cu at (47.9, 135.2)
- added D30: LTST-S270TBKT, led_matrix:LED_LiteOn_LTST-S270TBKT, F.Cu at (25.7, 75.1)
- added D300: LTST-S270TBKT, led_matrix:LED_LiteOn_LTST-S270TBKT, F.Cu at (91.9, 158.3)
- added D301: LTST-S270TBKT, led_matrix:LED_LiteOn_LTST-S270TBKT, F.Cu at (87.5, 162.5)
- added D302: LTST-S270TBKT, led_matrix:LED_LiteOn_LTST-S270TBKT, F.Cu at (83.1, 166.7)
- added D303: LTST-S270TBKT, led_matrix:LED_LiteOn_LTST-S270TBKT, F.Cu at (78.7, 170.9)
- added D304: LTST-S270TBKT, led_matrix:LED_LiteOn_LTST-S270TBKT, F.Cu at (74.3, 175.1)
- added D305: LTST-S270TBKT, led_matrix:LED_LiteOn_LTST-S270TBKT, F.Cu at (122.7, 137.3)
- added D306: LTST-S270TBKT, led_matrix:LED_LiteOn_LTST-S270TBKT, F.Cu at (65.5, 183.5)
- added D307: LTST-S270TBKT, led_matrix:LED_LiteOn_LTST-S270TBKT, F.Cu at (43.5, 206.6)
- added D308: LTST-S270TBKT, led_matrix:LED_LiteOn_LTST-S270TBKT, F.Cu at (47.9, 202.4)
- added D309: LTST-S270TBKT, led_matrix:LED_LiteOn_LTST-S270TBKT, F.Cu at (52.3, 198.2)
- added D31: LTST-S270TBKT, led_matrix:LED_LiteOn_LTST-S270TBKT, F.Cu at (65.5, 135.2)
- added D310: LTST-S270TBKT, led_matrix:LED_LiteOn_LTST-S270TBKT, F.Cu at (56.7, 194.0)
- added D311: LTST-S270TBKT, led_matrix:LED_LiteOn_LTST-S270TBKT, F.Cu at (61.1, 189.8)
- added D312: LTST-S270TBKT, led_matrix:LED_LiteOn_LTST-S270TBKT, F.Cu at (65.5, 185.6)
- added D313: LTST-S270TBKT, led_matrix:LED_LiteOn_LTST-S270TBKT, F.Cu at (118.3, 135.2)
- added D314: LTST-S270TBKT, led_matrix:LED_LiteOn_LTST-S270TBKT, F.Cu at (65.5, 187.7)
- added D315: LTST-S270TBKT, led_matrix:LED_LiteOn_LTST-S270TBKT, F.Cu at (61.1, 191.9)
- added D316: LTST-S270TBKT, led_matrix:LED_LiteOn_LTST-S270TBKT, F.Cu at (56.7, 196.1)
- added D317: LTST-S270TBKT, led_matrix:LED_LiteOn_LTST-S270TBKT, F.Cu at (52.3, 200.3)
- added D318: LTST-S270TBKT, led_matrix:LED_LiteOn_LTST-S270TBKT, F.Cu at (47.9, 204.5)
- added D319: LTST-S270TBKT, led_matrix:LED_LiteOn_LTST-S270TBKT, F.Cu at (43.5, 208.7)
- added D32: LTST-S270TBKT, led_matrix:LED_LiteOn_LTST-S270TBKT, F.Cu at (25.7, 79.6)
- added D320: LTST-S270TBKT, led_matrix:LED_LiteOn_LTST-S270TBKT, F.Cu at (69.9, 181.4)
- added D321: LTST-S270TBKT, led_matrix:LED_LiteOn_LTST-S270TBKT, F.Cu at (91.9, 152.0)
- added D322: LTST-S270TBKT, led_matrix:LED_LiteOn_LTST-S270TBKT, F.Cu at (78.7, 173.0)
- added D323: LTST-S270TBKT, led_matrix:LED_LiteOn_LTST-S270TBKT, F.Cu at (83.1, 168.8)
- added D324: LTST-S270TBKT, led_matrix:LED_LiteOn_LTST-S270TBKT, F.Cu at (87.5, 164.6)
- added D325: LTST-S270TBKT, led_matrix:LED_LiteOn_LTST-S270TBKT, F.Cu at (91.9, 160.4)
- added D326: LTST-S270TBKT, led_matrix:LED_LiteOn_LTST-S270TBKT, F.Cu at (96.3, 156.2)
- added D327: LTST-S270TBKT, led_matrix:LED_LiteOn_LTST-S270TBKT, F.Cu at (100.7, 152.0)
- added D328: LTST-S270TBKT, led_matrix:LED_LiteOn_LTST-S270TBKT, F.Cu at (105.1, 147.8)
- added D329: LTST-S270TBKT, led_matrix:LED_LiteOn_LTST-S270TBKT, F.Cu at (109.5, 143.6)
- added D33: LTST-S270TBKT, led_matrix:LED_LiteOn_LTST-S270TBKT, F.Cu at (47.9, 152.0)
- added D330: LTST-S270TBKT, led_matrix:LED_LiteOn_LTST-S270TBKT, F.Cu at (113.9, 139.4)
- added D331: LTST-S270TBKT, led_matrix:LED_LiteOn_LTST-S270TBKT, F.Cu at (118.3, 137.3)
- added D332: LTST-S270TBKT, led_matrix:LED_LiteOn_LTST-S270TBKT, F.Cu at (113.9, 141.5)
- added D333: LTST-S270TBKT, led_matrix:LED_LiteOn_LTST-S270TBKT, F.Cu at (109.5, 145.7)
- added D334: LTST-S270TBKT, led_matrix:LED_LiteOn_LTST-S270TBKT, F.Cu at (105.1, 149.9)
- added D335: LTST-S270TBKT, led_matrix:LED_LiteOn_LTST-S270TBKT, F.Cu at (100.7, 154.1)
- added D336: LTST-S270TBKT, led_matrix:LED_LiteOn_LTST-S270TBKT, F.Cu at (96.3, 158.3)
- added D337: LTST-S270TBKT, led_matrix:LED_LiteOn_LTST-S270TBKT, F.Cu at (91.9, 162.5)
- added D338: LTST-S270TBKT, led_matrix:LED_LiteOn_LTST-S270TBKT, F.Cu at (87.5, 166.7)
- added D339: LTST-S270TBKT, led_matrix:LED_LiteOn_LTST-S270TBKT, F.Cu at (83.1, 170.9)
- added D34: LTST-S270TBKT, led_matrix:LED_LiteOn_LTST-S270TBKT, F.Cu at (52.3, 147.8)
- added D340: LTST-S270TBKT, led_matrix:LED_LiteOn_LTST-S270TBKT, F.Cu at (78.7, 175.1)
- added D341: LTST-S270TBKT, led_matrix:LED_LiteOn_LTST-S270TBKT, F.Cu at (74.3, 179.3)
- added D342: LTST-S270TBKT, led_matrix:LED_LiteOn_LTST-S270TBKT, F.Cu at (69.9, 183.5)
- added D343: LTST-S270TBKT, led_matrix:LED_LiteOn_LTST-S270TBKT, F.Cu at (43.5, 210.8)
- added D344: LTST-S270TBKT, led_matrix:LED_LiteOn_LTST-S270TBKT, F.Cu at (47.9, 206.6)
- added D345: LTST-S270TBKT, led_matrix:LED_LiteOn_LTST-S270TBKT, F.Cu at (52.3, 202.4)
- added D346: LTST-S270TBKT, led_matrix:LED_LiteOn_LTST-S270TBKT, F.Cu at (56.7, 198.2)
- added D347: LTST-S270TBKT, led_matrix:LED_LiteOn_LTST-S270TBKT, F.Cu at (61.1, 194.0)
- added D348: LTST-S270TBKT, led_matrix:LED_LiteOn_LTST-S270TBKT, F.Cu at (65.5, 189.8)
- added D349: LTST-S270TBKT, led_matrix:LED_LiteOn_LTST-S270TBKT, F.Cu at (69.9, 185.6)
- added D35: LTST-S270TBKT, led_matrix:LED_LiteOn_LTST-S270TBKT, F.Cu at (56.7, 143.6)
- added D350: LTST-S270TBKT, led_matrix:LED_LiteOn_LTST-S270TBKT, F.Cu at (122.7, 135.2)
- added D351: LTST-S270TBKT, led_matrix:LED_LiteOn_LTST-S270TBKT, F.Cu at (69.9, 187.7)
- added D352: LTST-S270TBKT, led_matrix:LED_LiteOn_LTST-S270TBKT, F.Cu at (65.5, 191.9)
- added D353: LTST-S270TBKT, led_matrix:LED_LiteOn_LTST-S270TBKT, F.Cu at (61.1, 196.1)
- added D354: LTST-S270TBKT, led_matrix:LED_LiteOn_LTST-S270TBKT, F.Cu at (56.7, 200.3)
- added D355: LTST-S270TBKT, led_matrix:LED_LiteOn_LTST-S270TBKT, F.Cu at (52.3, 204.5)
- added D356: LTST-S270TBKT, led_matrix:LED_LiteOn_LTST-S270TBKT, F.Cu at (47.9, 208.7)
- added D357: LTST-S270TBKT, led_matrix:LED_LiteOn_LTST-S270TBKT, F.Cu at (43.5, 212.9)
- added D358: LTST-S270TBKT, led_matrix:LED_LiteOn_LTST-S270TBKT, F.Cu at (74.3, 181.4)
- added D359: LTST-S270TBKT, led_matrix:LED_LiteOn_LTST-S270TBKT, F.Cu at (78.7, 177.2)
- added D36: LTST-S270TBKT, led_matrix:LED_LiteOn_LTST-S270TBKT, F.Cu at (61.1, 139.4)
- added D360: LTST-S270TBKT, led_matrix:LED_LiteOn_LTST-S270TBKT, F.Cu at (83.1, 173.0)
- added D361: LTST-S270TBKT, led_matrix:LED_LiteOn_LTST-S270TBKT, F.Cu at (87.5, 168.8)
- added D362: LTST-S270TBKT, led_matrix:LED_LiteOn_LTST-S270TBKT, F.Cu at (91.9, 164.6)
- added D363: LTST-S270TBKT, led_matrix:LED_LiteOn_LTST-S270TBKT, F.Cu at (96.3, 160.4)
- added D364: LTST-S270TBKT, led_matrix:LED_LiteOn_LTST-S270TBKT, F.Cu at (100.7, 156.2)
- added D365: LTST-S270TBKT, led_matrix:LED_LiteOn_LTST-S270TBKT, F.Cu at (105.1, 152.0)
- added D366: LTST-S270TBKT, led_matrix:LED_LiteOn_LTST-S270TBKT, F.Cu at (109.5, 147.8)
- added D367: LTST-S270TBKT, led_matrix:LED_LiteOn_LTST-S270TBKT, F.Cu at (113.9, 143.6)
- added D368: LTST-S270TBKT, led_matrix:LED_LiteOn_LTST-S270TBKT, F.Cu at (118.3, 139.4)
- added D369: LTST-S270TBKT, led_matrix:LED_LiteOn_LTST-S270TBKT, F.Cu at (69.9, 179.3)
- renumbered R4 to R1, R5 to R2, R6 to R3
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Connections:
- DCDC1 pad 5: (no net) -> Net-(DCDC1-Pad5)
- J1 pad 2: (no net) -> Net-(J1-Pad2)
- J1 pad 3: (no net) -> Net-(J1-Pad3)
- J1 pad 4: (no net) -> Net-(J1-Pad4)
- MCU1 pad 1: (no net) -> Net-(MCU1-Pad1)
- MCU1 pad 10: (no net) -> Net-(MCU1-Pad10)
- MCU1 pad 100: (no net) -> Net-(MCU1-Pad100)
- MCU1 pad 11: (no net) -> Net-(MCU1-Pad11)
- MCU1 pad 12: (no net) -> Net-(MCU1-Pad12)
- MCU1 pad 13: (no net) -> Net-(MCU1-Pad13)
- MCU1 pad 14: (no net) -> Net-(MCU1-Pad14)
- MCU1 pad 15: (no net) -> Net-(MCU1-Pad15)
- MCU1 pad 16: (no net) -> Net-(MCU1-Pad16)
- MCU1 pad 17: (no net) -> Net-(MCU1-Pad17)
- MCU1 pad 18: (no net) -> Net-(MCU1-Pad18)
- MCU1 pad 19: (no net) -> Net-(MCU1-Pad19)
- MCU1 pad 2: (no net) -> Net-(MCU1-Pad2)
- MCU1 pad 20: (no net) -> Net-(MCU1-Pad20)
- MCU1 pad 21: (no net) -> Net-(MCU1-Pad21)
- MCU1 pad 22: (no net) -> Net-(MCU1-Pad22)
- MCU1 pad 23: (no net) -> Net-(MCU1-Pad23)
- MCU1 pad 24: (no net) -> Net-(MCU1-Pad24)
- MCU1 pad 25: (no net) -> Net-(MCU1-Pad25)
- MCU1 pad 26: (no net) -> Net-(MCU1-Pad26)
- MCU1 pad 27: (no net) -> Net-(MCU1-Pad27)
- MCU1 pad 28: (no net) -> Net-(MCU1-Pad28)
- MCU1 pad 29: (no net) -> Net-(MCU1-Pad29)
- MCU1 pad 3: (no net) -> Net-(MCU1-Pad3)
- MCU1 pad 30: (no net) -> Net-(MCU1-Pad30)
- MCU1 pad 31: (no net) -> Net-(MCU1-Pad31)
- MCU1 pad 32: (no net) -> Net-(MCU1-Pad32)
- MCU1 pad 33: (no net) -> Net-(MCU1-Pad33)
- MCU1 pad 34: (no net) -> Net-(MCU1-Pad34)
- MCU1 pad 35: (no net) -> Net-(MCU1-Pad35)
- MCU1 pad 36: (no net) -> Net-(MCU1-Pad36)
- MCU1 pad 37: (no net) -> Net-(MCU1-Pad37)
- MCU1 pad 38: (no net) -> Net-(MCU1-Pad38)
- MCU1 pad 39: (no net) -> Net-(MCU1-Pad39)
- MCU1 pad 4: (no net) -> Net-(MCU1-Pad4)
- MCU1 pad 40: (no net) -> Net-(MCU1-Pad40)
- MCU1 pad 41: (no net) -> Net-(MCU1-Pad41)
- MCU1 pad 42: (no net) -> Net-(MCU1-Pad42)
- MCU1 pad 43: (no net) -> Net-(MCU1-Pad43)
- MCU1 pad 44: (no net) -> Net-(MCU1-Pad44)
- MCU1 pad 45: (no net) -> Net-(MCU1-Pad45)
- MCU1 pad 46: (no net) -> Net-(MCU1-Pad46)
- MCU1 pad 47: (no net) -> Net-(MCU1-Pad47)
- MCU1 pad 48: (no net) -> Net-(MCU1-Pad48)
- MCU1 pad 49: (no net) -> Net-(MCU1-Pad49)
- MCU1 pad 5: (no net) -> Net-(MCU1-Pad5)
- MCU1 pad 50: (no net) -> Net-(MCU1-Pad50)
- MCU1 pad 51: (no net) -> Net-(MCU1-Pad51)
- MCU1 pad 52: (no net) -> Net-(MCU1-Pad52)
- MCU1 pad 53: (no net) -> Net-(MCU1-Pad53)
- MCU1 pad 54: (no net) -> Net-(MCU1-Pad54)
- MCU1 pad 55: (no net) -> Net-(MCU1-Pad55)
- MCU1 pad 56: (no net) -> Net-(MCU1-Pad56)
- MCU1 pad 57: (no net) -> Net-(MCU1-Pad57)
- MCU1 pad 58: (no net) -> Net-(MCU1-Pad58)
- MCU1 pad 59: (no net) -> Net-(MCU1-Pad59)
- MCU1 pad 6: (no net) -> Net-(MCU1-Pad6)
- MCU1 pad 60: (no net) -> Net-(MCU1-Pad60)
- MCU1 pad 61: (no net) -> Net-(MCU1-Pad61)
- MCU1 pad 62: (no net) -> Net-(MCU1-Pad62)
- MCU1 pad 63: (no net) -> Net-(MCU1-Pad63)
- MCU1 pad 64: (no net) -> Net-(MCU1-Pad64)
- MCU1 pad 65: (no net) -> Net-(MCU1-Pad65)
- MCU1 pad 66: (no net) -> Net-(MCU1-Pad66)
- MCU1 pad 67: (no net) -> Net-(MCU1-Pad67)
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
